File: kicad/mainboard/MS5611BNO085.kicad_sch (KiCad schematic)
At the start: 28 parts, among them U10 BNO085, U12 E220-900T22S(JP), U8 MS5611-01BA, Y2 32.768k

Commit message: 0.962 KiCad 更新、production を git 管理から外す
fabrication-toolkit が生成する production/ は発注のたびに作り直せるうえ、
基板を直すたびに巨大な差分になるので .gitignore に追加した。

Co-Authored-By: Claude Opus 5 <noreply@anthropic.com>
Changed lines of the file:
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@@
 		(dnp no)
 		(property "Reference" "JP1"
-			(at 114.046 56.388 0)
+			(at 103.378 55.118 0)
 			(show_name no)
 			(do_not_autoplace no)

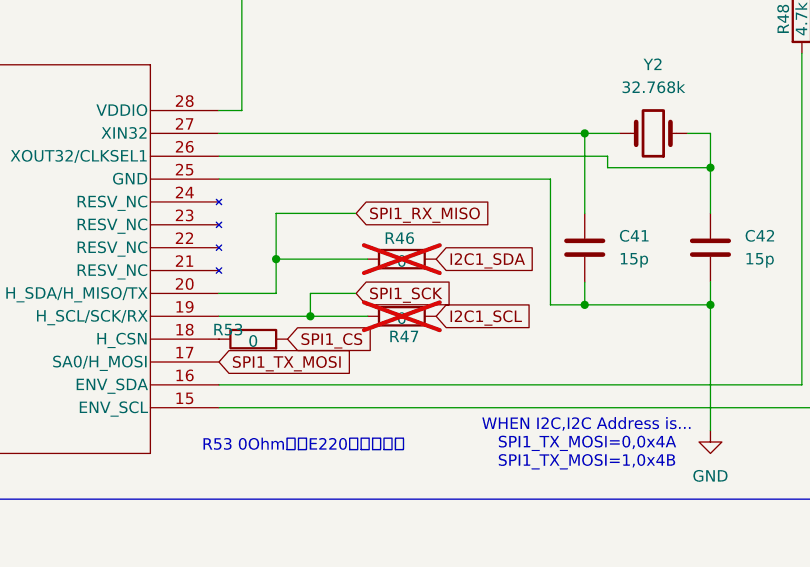
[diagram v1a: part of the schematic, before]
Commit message: 0.972 BNO085 のマウント変換を四元数化し、設定画面のフリーズを修正
v7 実機で BNO085 が動き出したことで出てきた不具合をまとめて直した。

- マウント補正を Euler の組み替えからクォータニオン回転へ。v7 は IC が基板裏面・
  1 番ピンが天という配置で、機体が水平のときセンサーがジンバルロック
  (sensor_pitch = ±90) に入る。角を入れ替える旧方式では原理的に直らない。
  変換は実機で静止時の生加速度（＝重力ベクトル）を 3 姿勢測って決め、
  settings.h の IMU_MOUNT_Q* 4 つに集約した。マウントを変えたら測り直して
  この 4 つを差し替えるだけでよい。
  ピッチの符号も機首上げ正へ直した（ZYX 抽出がそのまま返すのは機首下げ正）。
- 変換の写しを全廃。imu.cpp / attitude.cpp / decode_imulog.py / eskf.py /
  attitude_test の 5 箇所に同じ式が散っており、片方だけ直すと静かにずれていた。
  実体は attitude.h の imu_body_euler_rad() と mount_correct_quat() の 2 つだけ。
  attitude_test は合成データをセンサー座標で流す形に直したので、出力ロールを
  そのまま真のバンクと比較する（細工した量どうしの比較をやめた）。
- 設定画面のフリーズを修正。WIRELESS 画面の「戻る」が独自 switch で早期 return
  するため値変更モードが解除されず、次の短押しで null の CallbackToggle を呼び
  std::bad_function_call で停止していた。呼ぶ側でも null を弾くようにした。
- WIRELESS 画面が地図専用の push_backscreen() を呼んでいたのをやめた。y=50 に
  置くため 20px の隙間に前の画面が残り、フッタは誰も消さず、受信モードでは
  受信枠の矩形が設定の上に描かれていた。
- BNO085 の CS をリセット前から HIGH に固定。基板に H_CSN のプルアップが無く、
  NRST〜ブート 400ms の間 CS が浮いて起動しなかった（実機初回通電で判明）。
- begin 失敗時に stage/INT/RST/PS0 を残す。「チップが居ない」と「配線が違う」で
  対処が正反対なので、log.txt だけで切り分けられるようにした。
- 設定読み込み完了をログに残す（SETTINGS LOADED と LINK SETUP の settings=）。

Co-Authored-By: Claude Opus 5 <noreply@anthropic.com>
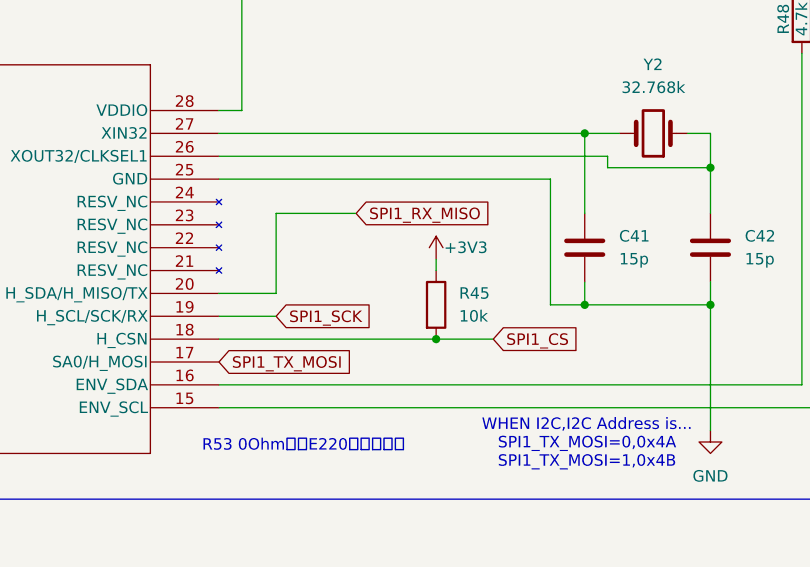
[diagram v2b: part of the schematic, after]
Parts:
- removed R46, R47, R53: 0, Resistor_SMD:R_0603_1608Metric_Pad0.98x0.95mm_HandSolder, symbol Device:R
- added R45: 10k, Resistor_SMD:R_0402_1005Metric, symbol Device:R
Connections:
- net +3V3: now also R45.1
- net SPI1_CS: now also U10.18 (H_CSN), R45.2

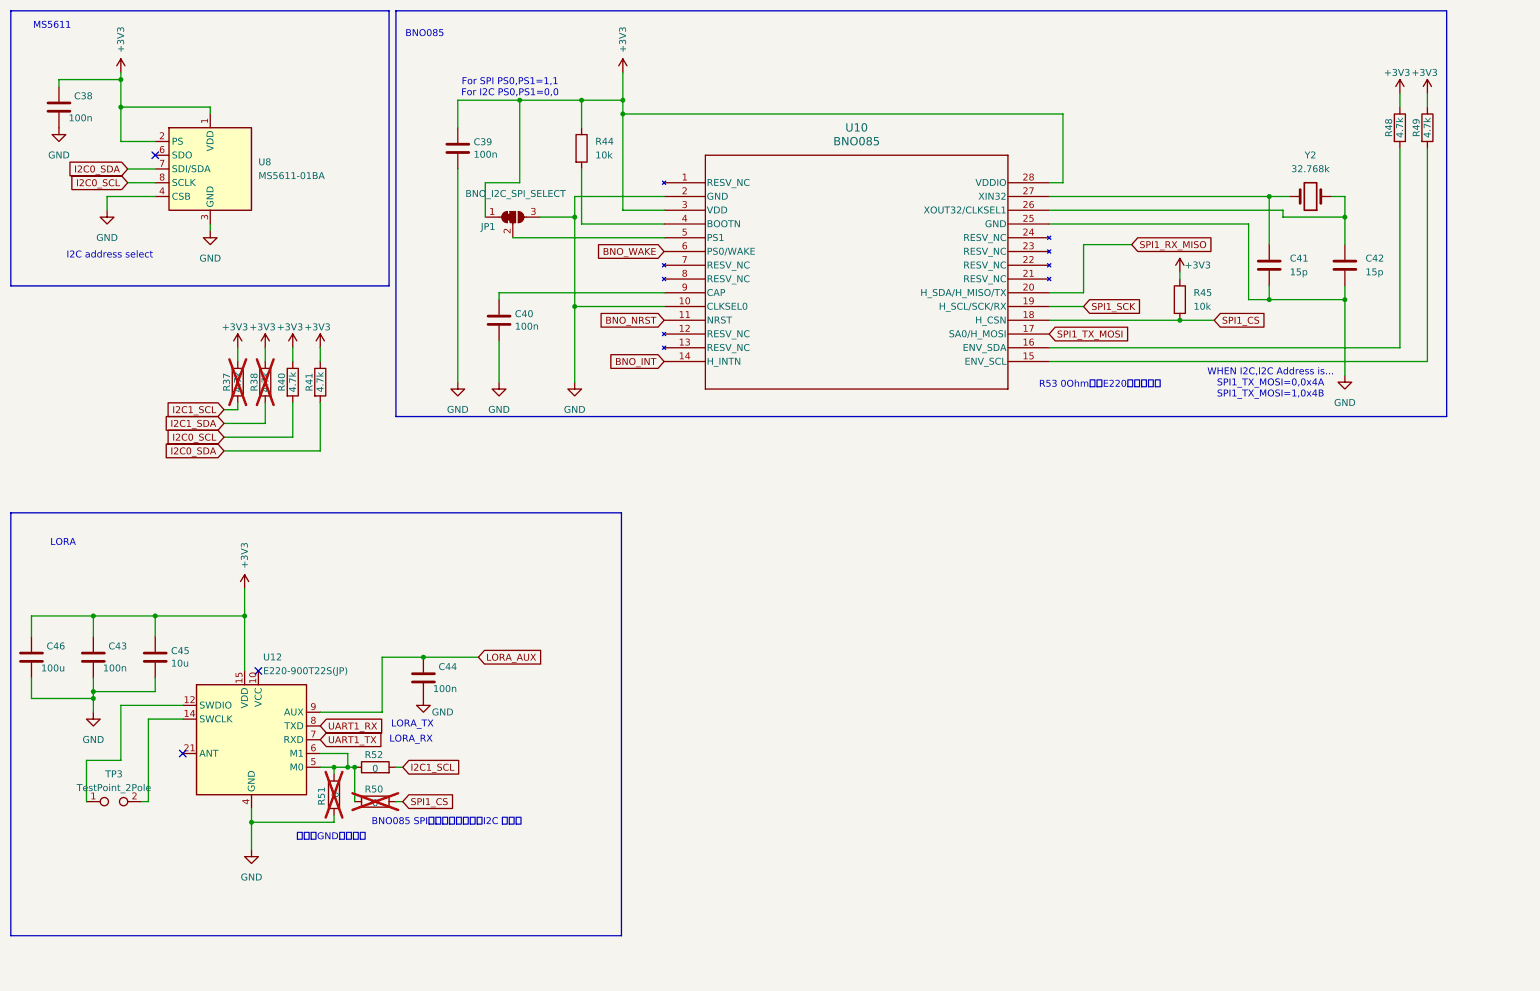
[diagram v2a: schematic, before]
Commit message: 0.986 新基板（SCH16T 外付け）の kicad を追加し、ガーバー出力を git から外した
kicad/IMU_murata/ — SCH16T-K01-10 のブレイクアウト（新規）
本体の J7（Molex 200528-0080・8pin FPC）へ 1:1 ケーブルで繋ぐ外付け基板。
J1 のピン順を本体 J7 と一致させてある（1=+3V3 2=RESET 3=MOSI 4=CS 5=SCK
6=SYNC 7=MISO 8=GND）。シンボルとフットプリントも同梱。
- ★ R2（CS-GND の 4.7k）は実装しない。CS は負論理なので、プルダウンすると
  MCU が駆動していない間セレクト状態になる。R1（EXTRESN プルアップ）は実装する
- 本体側の GPIO 割り当ては settings.h の SCH16T_PIN_* が正本
  （一覧は docs/imu_sch16t_plan.md §3）

mainboard / GNSS モジュールの更新
- mainboard: DisplayModule_PONSv7 の pcb / pro / sch、MS5611BNO085.kicad_sch、
  SHT_RP2354B.kicad_sch
- GNSS モジュール: pcb / pro / sch、および QRv7 と FPC 4p のフットプリントを
  同プロジェクトの Footprints/ へ取り込み

kicad/FPC/ を畳んだ
FPC コネクタ 1 個のためのプロジェクトだったので、フットプリントを
kicad/GNSSboard_SAM-M10Q/Footprints/ へ移して削除した。
中身は同じで、差分は KiCad が再生成する uuid だけ。

ガーバー・ドリルのプロット出力を git から外した
kicad/.gitignore に追加（*.gbr *.gbl *.gbs *.gbp *.gbo *.gm1 *.gtl *.gts
*.gtp *.gto *.drl と、保険の *plot/ *plot.zip）。発注のたびに作り直せるうえ、
基板を直すたびに巨大な差分になる（ルート .gitignore の production/ と同じ理由）。
★ 入れ物のフォルダ名で書かないこと。v5_1plot/ のような名前は付け方が毎回違うので
  次の基板で外れる。既存の *-backups/ / *.kicad_prl と同じ方針。

Co-Authored-By: Claude Opus 5 <noreply@anthropic.com>
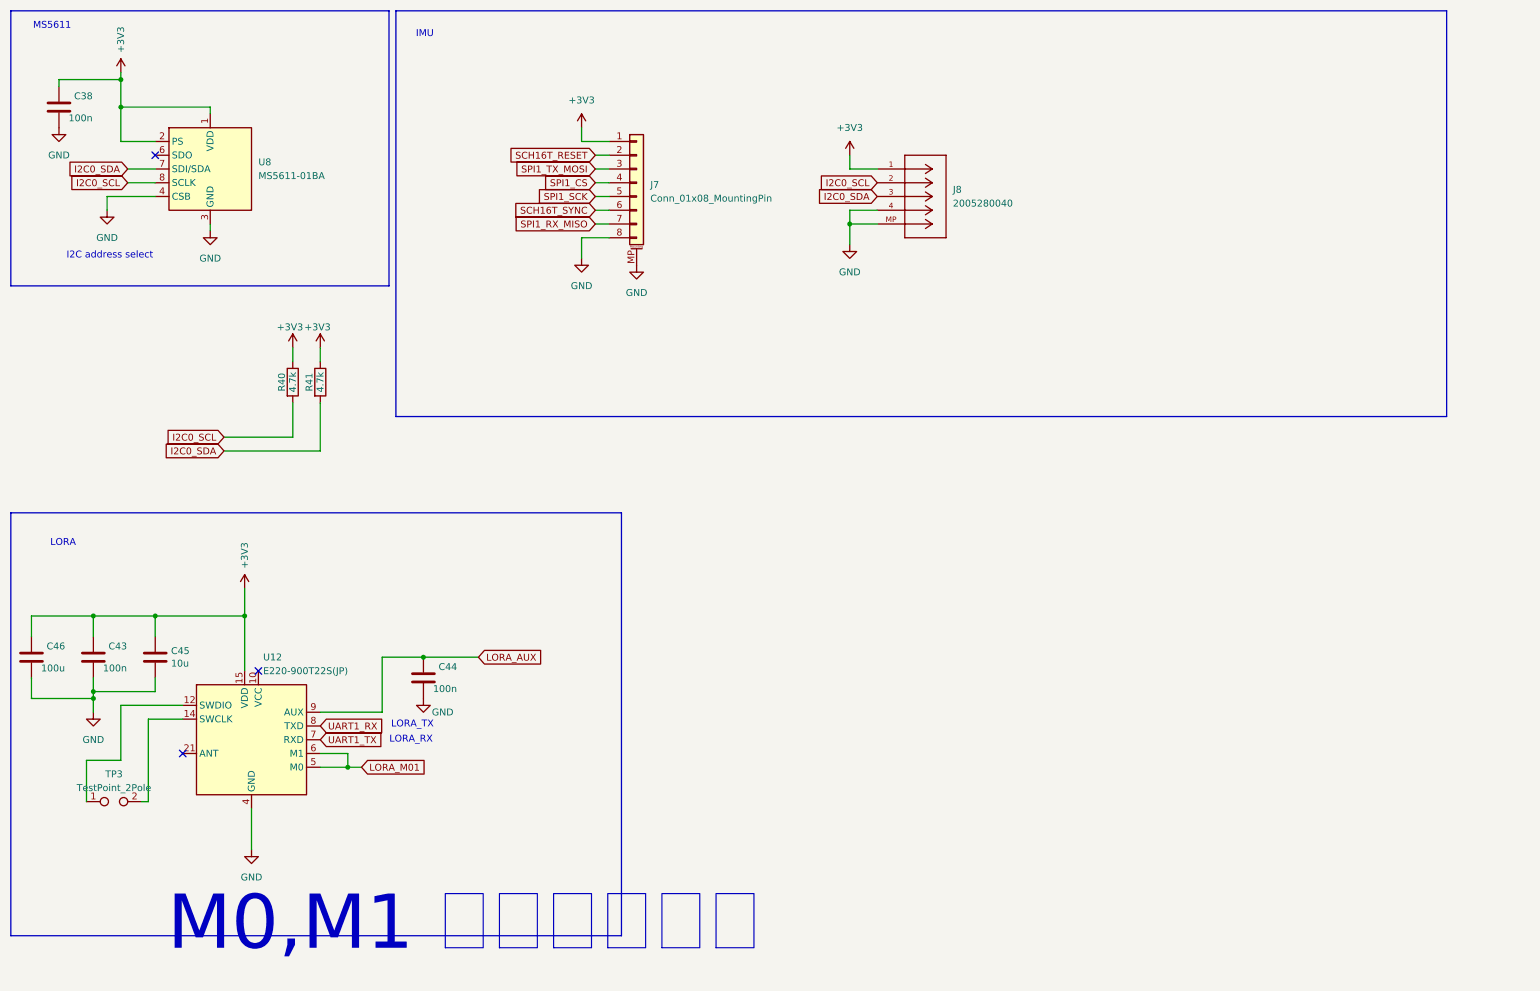
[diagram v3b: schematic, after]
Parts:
- removed C39, C40: 100n, GPS_TFT:C_0402_1005Metric_small_pads, symbol Device:C
- removed C41, C42: 15p, GPS_TFT:C_0402_1005Metric_small_pads, symbol Device:C
- removed JP1: BNO_I2C_SPI_SELECT, Jumper:SolderJumper-3_P1.3mm_Bridged2Bar12_Pad1.0x1.5mm, symbol Jumper:SolderJumper_3_Bridged12
- removed R37, R38: 4.7k, Resistor_SMD:R_0603_1608Metric_Pad0.98x0.95mm_HandSolder, symbol Device:R
- removed R44, R45: 10k, Resistor_SMD:R_0402_1005Metric, symbol Device:R
- removed R48, R49: 4.7k, Resistor_SMD:R_0402_1005Metric, symbol Device:R
- removed R50, R51, R52: 0, Resistor_SMD:R_0603_1608Metric_Pad0.98x0.95mm_HandSolder, symbol Device:R
- removed U10: BNO085, GPS_TFT:bno085, symbol bno085:BNO085
- removed Y2: 32.768k, Crystal:Crystal_SMD_3215-2Pin_3.2x1.5mm, symbol Device:Crystal
- added J7: Conn_01x08_MountingPin, Connector_FFC-FPC:Molex_200528-0080_1x08-1MP_P1.00mm_Horizontal, symbol Connector_Generic_MountingPin:Conn_01x08_MountingPin
- added J8: 2005280040, Connector_FFC-FPC:Molex_200528-0040_1x04-1MP_P1.00mm_Horizontal, symbol 2005280040:2005280040
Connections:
- net +3V3: now also J7.1 (Pin_1), J8.1
- net GND: now also J7.8 (Pin_8), J7.MP (MountPin), J8.4, J8.MP
- net I2C0_SCL: now also J8.2
- net I2C0_SDA: now also J8.3
- net SPI1_CS: now also J7.4 (Pin_4)
- net SPI1_RX_MISO: now also J7.7 (Pin_7)
- net SPI1_SCK: now also J7.5 (Pin_5)
- net SPI1_TX_MOSI: now also J7.3 (Pin_3)
- net LORA_M01: now reaches U12.5 (M0), U12.6 (M1)
- new net SCH16T_RESET: J7.2 (Pin_2)
- new net SCH16T_SYNC: J7.6 (Pin_6)
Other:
- note added: "IMU"
- note added: "M0,M1 ピン変更あり"
- note removed: "BNO085"
- note removed: "BNO085 SPI本命、失敗したらI2C 使う。"
- note removed: "For SPI PS0,PS1=1,1 For I2C PS0,PS1=0,0"
- note removed: "R53 0Ohmは、E220のために。"
- note removed: "WHEN I2C,I2C Address is... SPI1_TX_MOSI=0,0x4A SPI1_TX_MOSI=1,0x4B"
- note removed: "念の為GND直結残す"

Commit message: 0.993 v7.1 基板の回路図と PCB を仕上げ、SW OFF のままの充電と電源異常を画面と音声で知らせるようにした
- power.cpp（新規）: USB の判定を usb_power_present() に一本化（v7.1 は VBUS を
  GPIO47 の ADC で測る）。電源経路の異常（2026-10-15 の充電 IC 焼損）を検出し、
  地図の POWER FAULT!! と power_fault.wav（30 秒ごと・最低音量 60）で知らせる。
  受信機は LINK_ST_PWR_FAULT を受けてトーン（同じ音声だとボートへの指示に聞こえる）
- v7.1: SW を OFF にしたまま USB で充電していると満充電にならない（Q3 のボディ
  ダイオード経由）。SW4 の OFF 側が GPIO40 を GND に落とすのを読み、地図に注意を出し
  1 度だけ読み上げる（charge_sw_off / charge_sw_on。排他グループ WAV_EXCL_CHARGE_SW）。
  移動中・ミラー中・リプレイ中・デモ中は出さない。判定に USB を入れない
  （VBUS が一瞬 4.3V を割ると 0V が本物の電池電圧として流れるため）。このあいだは
  電池低下の警告を止め、無線は RHAVE_VOLT を立てず LINK_ST_USB_SW_OFF、CSV は空欄
- 受信モードの電池表示を s55r42 の形に。SW OFF のまま USB の側は s5V / r5V
- backlight.cpp（新規）: v7.1 のバックライト PWM と VEML7700 の自動調光。
  飛行 CSV に lux / backlight 列
- E220 の M0/M1 は v7.1 で GPIO31 へ（GPIO47 は USB_SENS）
- 本体の回路図・PCB: SCH16T の J6 を逆順に（完成済みの FPC で J6-n ↔ J3-(9-n)）、
  F1 0805L035 → 0805L050（夏の充電で切れない）、R34/R35 を 10k/5.1k、C32 を 10µF 0805、
  SPI1 の SCK/MOSI/CS に 33Ω（R49〜R51）、スライドスイッチを MST-12D18G2 に、
  回路図とつながらない旧フットプリント（C33/R37/R38/R11 470Ω）を削除、DNP の BOM 除外、
  CUS-12TB の残骸とライブラリ登録を削除、メモの部品番号を v7.1 に
- GNSS 基板を 5 ピン（V_BCKUP）に。バックアップ電池は本体へ移した
- case_cover（照度センサー VEML7700）の kicad を追加。IMU ブレイクアウトの R2 を DNP
- 音声 3 本（power_fault / charge_sw_off / charge_sw_on）は macOS の音声合成の仮音声
- docs/pons_power.md（新規）。README の「自作の手順」を v7.1 に書き直し、
  SCH16T の配線の記述（J7・1:1 ケーブル）を J6・逆順に直した
- gen_wav_flash.py はコメント中の引用符付きの音声名も拾うので、録音前の名前を書かない

PONS_BOARD は V7 と V71 の両方でビルド OK（3,929,776 / 3,923,504 B）/
gen_wav_flash.py --check は 35 ファイル一致 / 本体 PCB の DRC は未配線 0・回路図と一致
（シルクの 6 件はボタンと USB の突起で意図どおり）/ GNSS 基板も未配線 0 / 実機は未確認

Co-Authored-By: Claude Opus 5.5 <noreply@anthropic.com>
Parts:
- added BT1: MS621FE, Battery:BatteryHolder_Seiko_MS621F, symbol Device:Battery_Cell
- added C47, C48: 100n, GPS_TFT:C_0402_1005Metric_small_pads, symbol Device:C
- added D5: RB520S-30, Diode_SMD:D_SOD-523, symbol Diode:1N4001
- added J7: 2005280050, Connector_FFC-FPC:Molex_200528-0050_1x05-1MP_P1.00mm_Horizontal, symbol Connector_Generic_MountingPin:Conn_01x05_MountingPin
- added R43: 220, Resistor_SMD:R_0402_1005Metric, symbol Device:R
- added R44: 470, Resistor_SMD:R_0402_1005Metric, symbol Device:R
- added R49, R50, R51: 33, Resistor_SMD:R_0402_1005Metric, symbol Device:R
- J6: renamed from J7; now left out of the parts list
- J8: LCSC C563728 -> (none); now left out of the parts list
- renumbered C46 to C42, C38 to C43, C43 to C44, C44 to C46, R40 to R41, R41 to R42, TP3 to TP1, U12 to U9
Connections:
- net +3V3: now also J6.8 (Pin_8), C48.1, J7.1 (Pin_1), R43.1; no longer J6.1 (Pin_1)
- net GND: now also J6.1 (Pin_1), BT1.2 (-), C47.2, C48.2, J7.2 (Pin_2), J7.MP (MountPin); no longer J6.8 (Pin_8)
- net SCH16T_RESET: now also J6.7 (Pin_7); no longer J6.2 (Pin_2)
- net SCH16T_SYNC: now also J6.3 (Pin_3); no longer J6.6 (Pin_6)
- net SPI1_CS: now also R50.1; no longer J6.4 (Pin_4)
- net SPI1_RX_MISO: now also J6.2 (Pin_2); no longer J6.7 (Pin_7)
- net SPI1_SCK: now also R49.1; no longer J6.5 (Pin_5)
- net SPI1_TX_MOSI: now also R51.1; no longer J6.3 (Pin_3)
- new net: BT1.1 (+), R44.2
- new net: J6.4 (Pin_4), R49.2
- new net: J6.5 (Pin_5), R50.2
- new net: J6.6 (Pin_6), R51.2
- new net: D5.2 (A), R43.2
- new net UART0_RX: J7.3 (Pin_3)
- new net UART0_TX: J7.4 (Pin_4)
- new net V_BCKUP: C47.1, D5.1 (K), J7.5 (Pin_5), R44.1
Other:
- note added: "BT1が放電しきっていると、モジュールが起動しないバグがあった。 V_BCKP Minimum operating voltage = 1.65V R2抵抗によって、BT1バッテリーが空っぽでも、V_BCKUPに電圧が生じる((3.3-0.6)*470/690)=1.8Vぐらい 放電時は、R2の電圧降下はV=IR=10*10^-6*470 で、電圧降下はほとんどない P=IV=V^2/R=(0.5*10^-3)^2/500=0.5*10^-9=0.5nW"
- note added: "EXTERNAL CONNECTORS"
- note added: "GNSS CONNECTOR Socket substitute:0522710479"
- note added: "I2C(AMBIENT LIGHT SENSOR VEML7700)"
- note added: "突入電流&バッテリー電流制限&最小 V_BCKP 対策"
